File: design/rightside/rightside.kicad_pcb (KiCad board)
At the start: 4 copper layers, 144 x 95.2 mm, 167 parts, among them IC2 XC9148G50CER-G, IC3 nRF52833-QDAA-R7, IC4 74AHCT125PW,118, IC5 MCP23018T-E_SS, IC6 XC9291B33D1R-G, J1 USB_C_Receptacle_USB2.0_16P, J2 Battery Pos, J3 Battery Neg, J4 OLED_128x32, J5 SFV12R-1STBE1HLF, J6 PinHeader_1x04_P2.54mm_Horizo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, U2 BQ24072RGT, U3 USB6B1, U4 BQ27441-G1, U5 PEC11L-4015F-S0015, U6 PEC11L-4015F-S0015, X1 32MHz

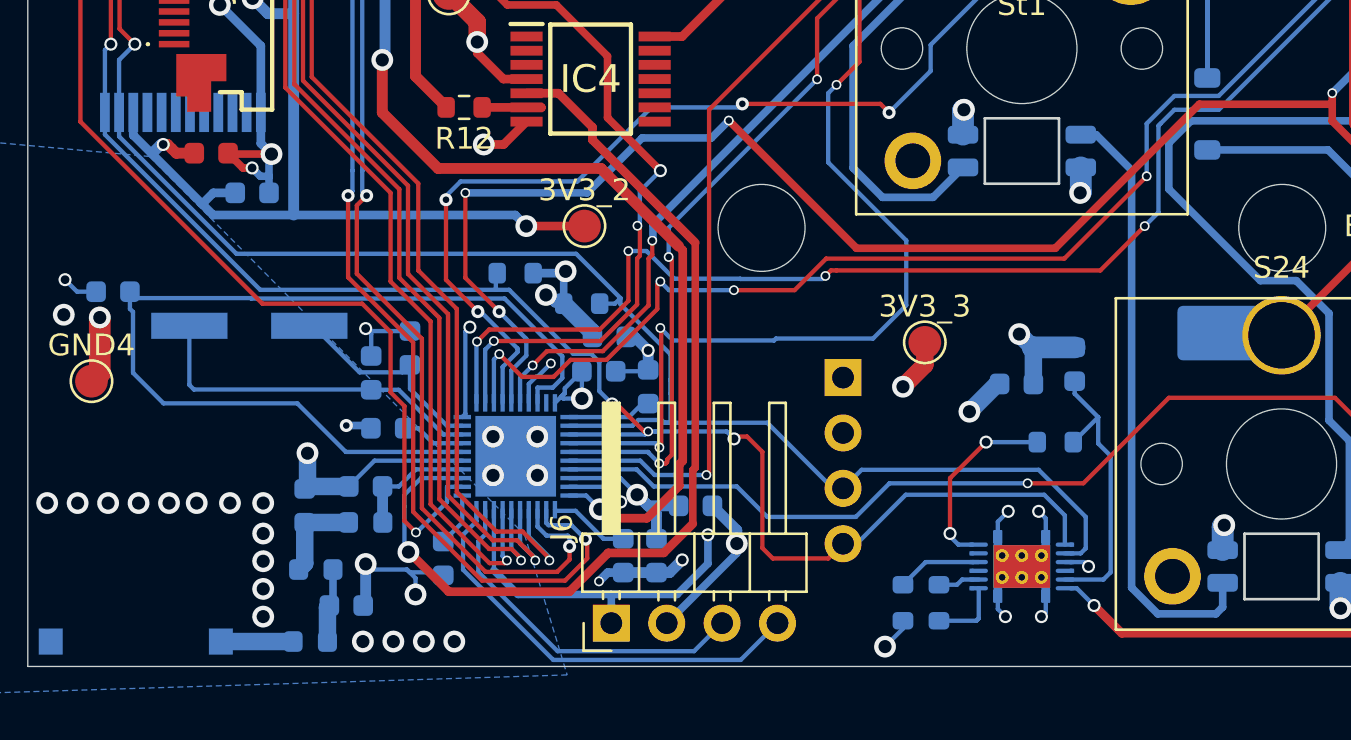
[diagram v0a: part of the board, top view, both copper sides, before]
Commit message: correct fuel gauge and crystal
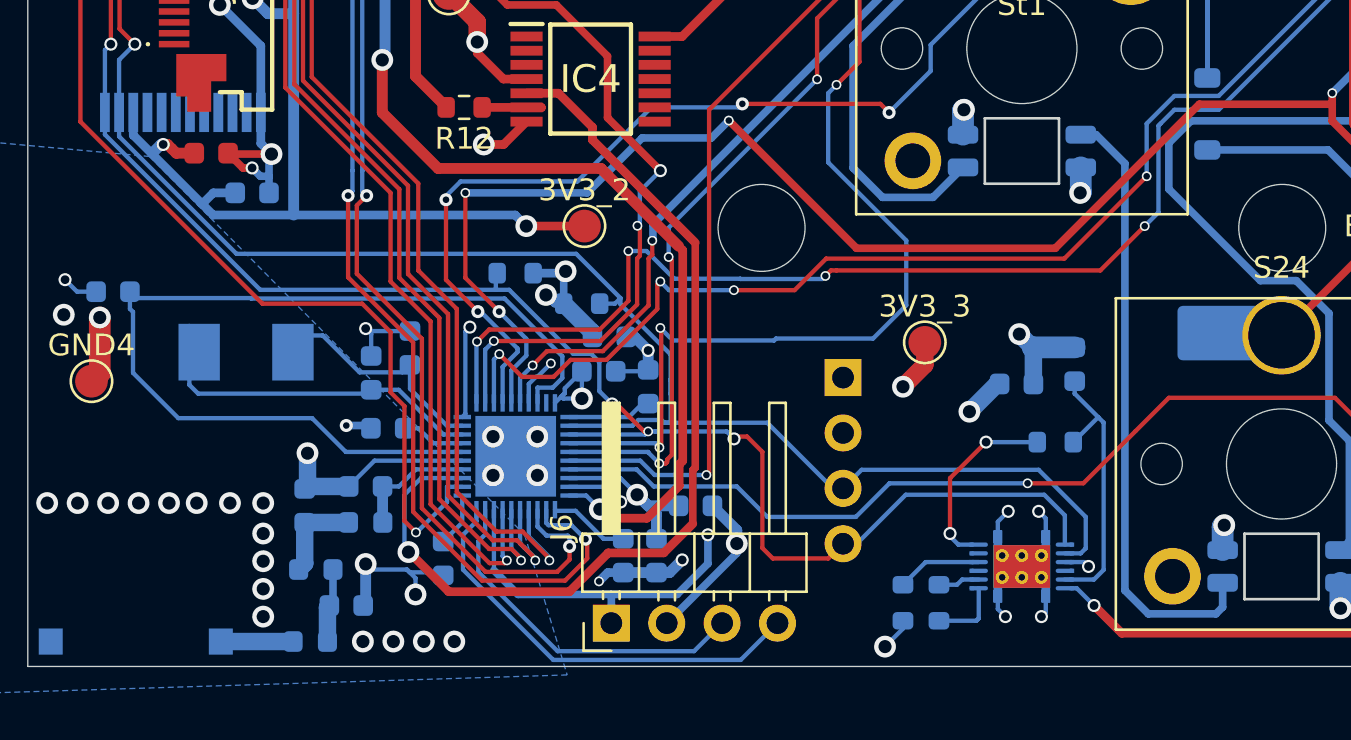
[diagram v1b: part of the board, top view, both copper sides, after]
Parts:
- removed X1: 32MHz, Crystal:Crystal_SMD_ECS_CSM3X-2Pin_7.6x4.1mm
- added Y1: ABM7-32.000MHZ-D2Y-T, SamacSys_Parts:ABM7, B.Cu at (69.2, 107.6)
- J6: value PinHeader_1x04_P2.54mm_Horizontal -> Conn_01x04
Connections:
- J6 pad 3: Net-(IC3-SWDIO) -> Net-(IC3-SWDCLK)
- J6 pad 4: Net-(IC3-SWDCLK) -> Net-(IC3-SWDIO)
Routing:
- net Net-(IC3-XC1): track 16.2 -> 17.2 mm
- net Net-(IC3-XC2): track 9.84 -> 10.7 mm
- net Net-(U4-V_{DD}): track 13.3 -> 12.8 mm

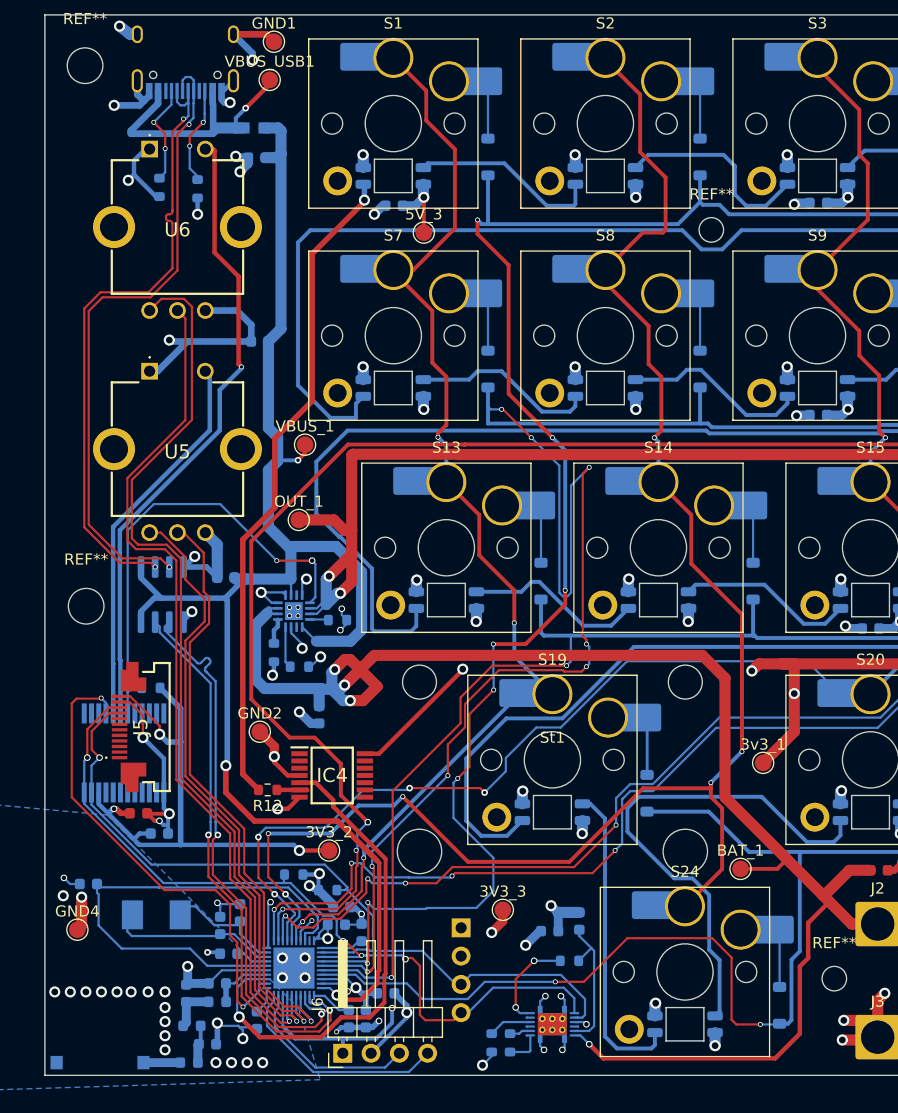
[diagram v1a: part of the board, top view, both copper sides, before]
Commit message: prepare to reroute
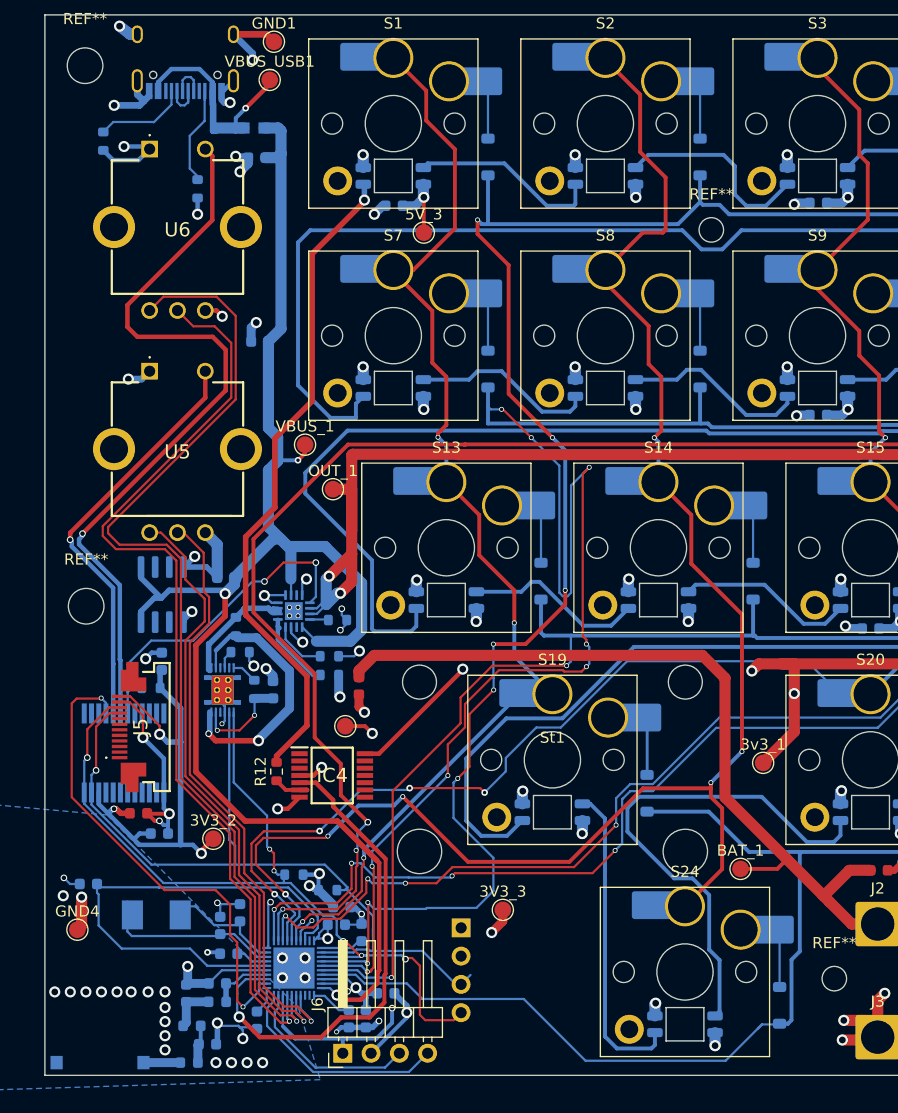
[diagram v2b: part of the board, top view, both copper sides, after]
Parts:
- C17: moved to F.Cu
- Y1: value ABM7-32.000MHZ-D2Y-T -> 32 MHz
- moved R9 44.8 mm to (76.4, 81.7), turned to 90 degrees
- moved C9 42.4 mm to (69.7, 84.8), turned to 90 degrees
- moved U4 42.2 mm to (75.2, 87.4), turned to 90 degrees
- moved R7 41.7 mm to (76.7, 84.0), turned to 0 degrees
- moved R8 37.4 mm to (78.0, 87.3), turned to -90 degrees
- moved C22 34.5 mm to (79.7, 87.4)
- moved 3V3_2 10.5 mm to (74.3, 100.8)
- moved GND2 7.70 mm to (86.2, 90.6)
- moved R1 6.53 mm to (64.4, 38.1)
- moved R5 5.38 mm to (84.8, 86.0), turned to 180 degrees
- moved C17 4.42 mm to (87.4, 87.0)
- moved OUT_1 4.13 mm to (85.1, 69.4)
- moved R4 2.85 mm to (84.8, 84.4)
- moved R12 1.83 mm to (80.0, 94.7), turned to 90 degrees
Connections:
- J6 pad 3: Net-(IC3-SWDCLK) -> Net-(IC3-SWDIO)
- J6 pad 4: Net-(IC3-SWDIO) -> Net-(IC3-SWDCLK)
- R7 pad 1: GND -> Net-(U4-BIN)
- R7 pad 2: Net-(U4-BIN) -> GND
- R9 pad 1: Net-(U4-SRP) -> /BAT
- R9 pad 2: Net-(U4-SRN) -> /BAT_SRN
- U2 pad 2: /BAT -> /BAT_SRN
- U2 pad 3: /BAT -> /BAT_SRN
- U4 pad 7: Net-(U4-SRN) -> /BAT_SRN
- U4 pad 8: Net-(U4-SRP) -> /BAT
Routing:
- net /D_P: track 57.5 -> 3.18 mm, vias 2 -> 0
- net /D_N: track 57.5 -> 4.30 mm, vias 2 -> 0
- net D-: track 50.3 -> 0.00 mm, vias 2 -> 0
- net D+: track 50.2 -> 0.00 mm, vias 2 -> 0
- net /BAT: track 142.4 -> 98.4 mm, vias 4 -> 2
- net GND: track 241.7 -> 225.4 mm
- net /NO2: track 56.3 -> 68.7 mm
- net /BAT_SRN: track 0.00 -> 11.8 mm
- net 3V3: track 266.5 -> 256.7 mm, vias 14 -> 13
- net /CCW2: track 81.7 -> 89.7 mm
- net /CW2: track 76.9 -> 84.3 mm
- net Net-(U4-GPOUT): track 8.50 -> 2.31 mm, vias 2 -> 0
- net /VBUS_USB: track 24.9 -> 19.8 mm
- net Net-(U2-TS): track 2.38 -> 7.24 mm
- net /SDA: track 73.4 -> 78.1 mm, vias 4 -> 6
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
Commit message: prepare to make test board
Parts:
- removed L4: 4.3nH, Inductor_SMD:L_0603_1608Metric
- removed R10, R11, R6: 10k, Resistor_SMD:R_0603_1608Metric
- removed the REF** at (130.1, 113.3)
- removed the REF** at (62.8, 31.3)
- removed the REF** at (199.5, 35.8)
- removed the REF** at (62.9, 79.9)
- added C24: 4.7uF, ScottoKeebs_Components:Capacitor_0603, B.Cu at (78.4, 39.6)
- added C38: 100nF, ScottoKeebs_Components:Capacitor_0603, B.Cu at (83.3, 120.4)
- added C39: 100nF, ScottoKeebs_Components:Capacitor_0603, F.Cu at (82.2, 118.1)
- added REF**: MountingHole_2.2mm_M2, MountingHole:MountingHole_2.2mm_M2, F.Cu at (62.0, 80.1)
- added REF**: MountingHole_2.2mm_M2, MountingHole:MountingHole_2.2mm_M2, F.Cu at (200.2, 35.6)
- added REF**: MountingHole_2.2mm_M2, MountingHole:MountingHole_2.2mm_M2, F.Cu at (130.0, 113.6)
- added REF**: MountingHole_2.2mm_M2, MountingHole:MountingHole_2.2mm_M2, F.Cu at (200.3, 100.9)
- added REF**: MountingHole_2.2mm_M2, MountingHole:MountingHole_2.2mm_M2, F.Cu at (63.0, 31.2)
- C35: value 22uF -> 100nF; moved to F.Cu
- C36: value 1.5pF -> 100nF; moved to F.Cu
- F1: value 500mA -> 600mA
- moved C35 60.9 mm to (71.3, 100.1), turned to -90 degrees
- moved C18 57.2 mm to (78.5, 90.4), turned to 90 degrees
- moved C9 35.6 mm to (94.5, 110.4)
- moved C36 19.1 mm to (73.5, 100.1), turned to -90 degrees
- moved 3V3_2 11.1 mm to (85.3, 102.2)
- moved 3V3_3 6.32 mm to (102.1, 113.2)
- moved C17 4.26 mm to (89.6, 83.4), turned to 180 degrees
- moved C11 3.35 mm to (75.4, 118.8)
- moved L2 2.55 mm to (71.6, 120.0), turned to 90 degrees
- moved R2 2.52 mm to (75.4, 42.0)
- moved C15 0.93 mm to (71.6, 115.5)
- moved C16 0.88 mm to (75.5, 113.5)
- moved C19 0.76 mm to (74.2, 108.8)
- moved C20 0.76 mm to (68.8, 100.1)
- moved C8 0.40 mm to (85.5, 106.9)
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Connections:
- ANT1 pad 1: Net-(ANT1-FEED) -> /RF
- C35 pad 1: /VBUS -> GND
- C35 pad 2: GND -> 3V3
- C36 pad 1: /RF -> GND
- C36 pad 2: GND -> 3V3
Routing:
- net D-: track 0.00 -> 52.6 mm, vias 0 -> 2
- net D+: track 0.00 -> 52.6 mm, vias 0 -> 2
- net /D_P: track 3.18 -> 55.1 mm
- net /D_N: track 4.30 -> 55.1 mm
- net 3V3: track 256.7 -> 241.7 mm, vias 13 -> 15
- net /CHG: track 38.0 -> 29.9 mm, vias 2 -> 4
- net /2A: track 44.6 -> 50.8 mm
- net /BAT: track 98.4 -> 104.3 mm, vias 2 -> 3
- net GND: track 225.4 -> 220.6 mm, vias 115 -> 126
- net Net-(IC3-DEC5): track 2.47 -> 6.16 mm
- net Net-(ANT1-FEED): track 3.31 -> 0.00 mm
- net /Row 3: track 165.2 -> 162.6 mm
- net /SCL: track 73.0 -> 70.7 mm
- net /INTA: track 44.1 -> 46.0 mm
- net /VBUS_USB: track 19.8 -> 18.1 mm
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- added copper zone on B.Cu, net D+
- added copper zone on B.Cu, net D-
